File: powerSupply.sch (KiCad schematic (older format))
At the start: 40 parts, among them U10 TPS7A4901, U11 LM3880, U12 TPS7A3001, U13 TPS7A3001, U8 TPS7A4901, U9 TPS7A4901

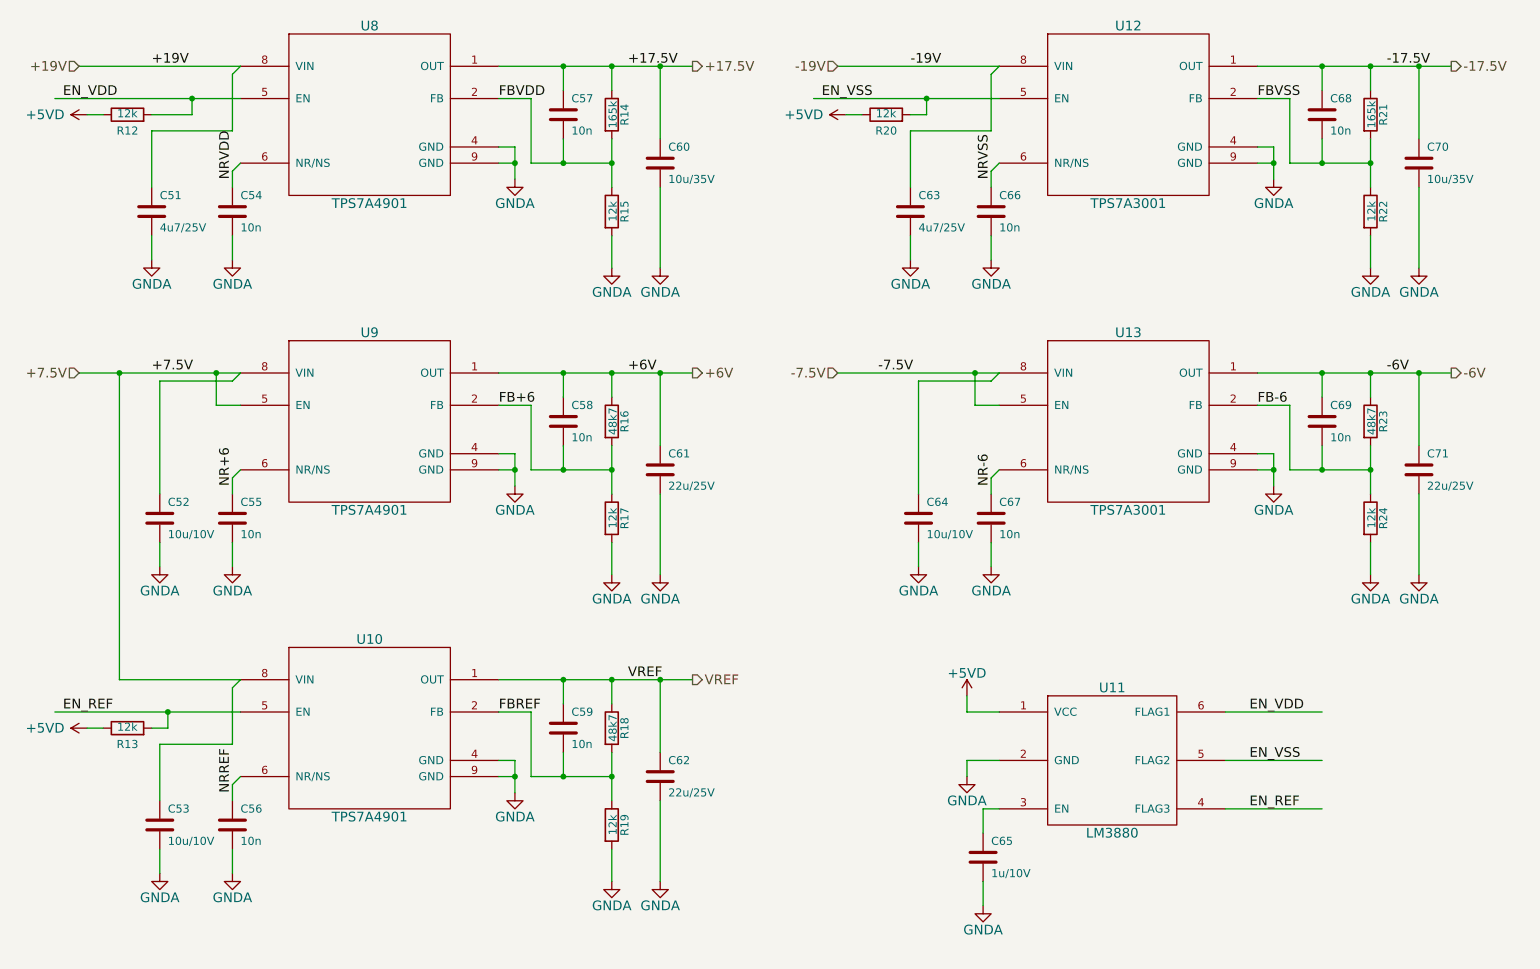
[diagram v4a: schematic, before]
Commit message: Expanded the board for better grounding. OP-AMPs close to connectors
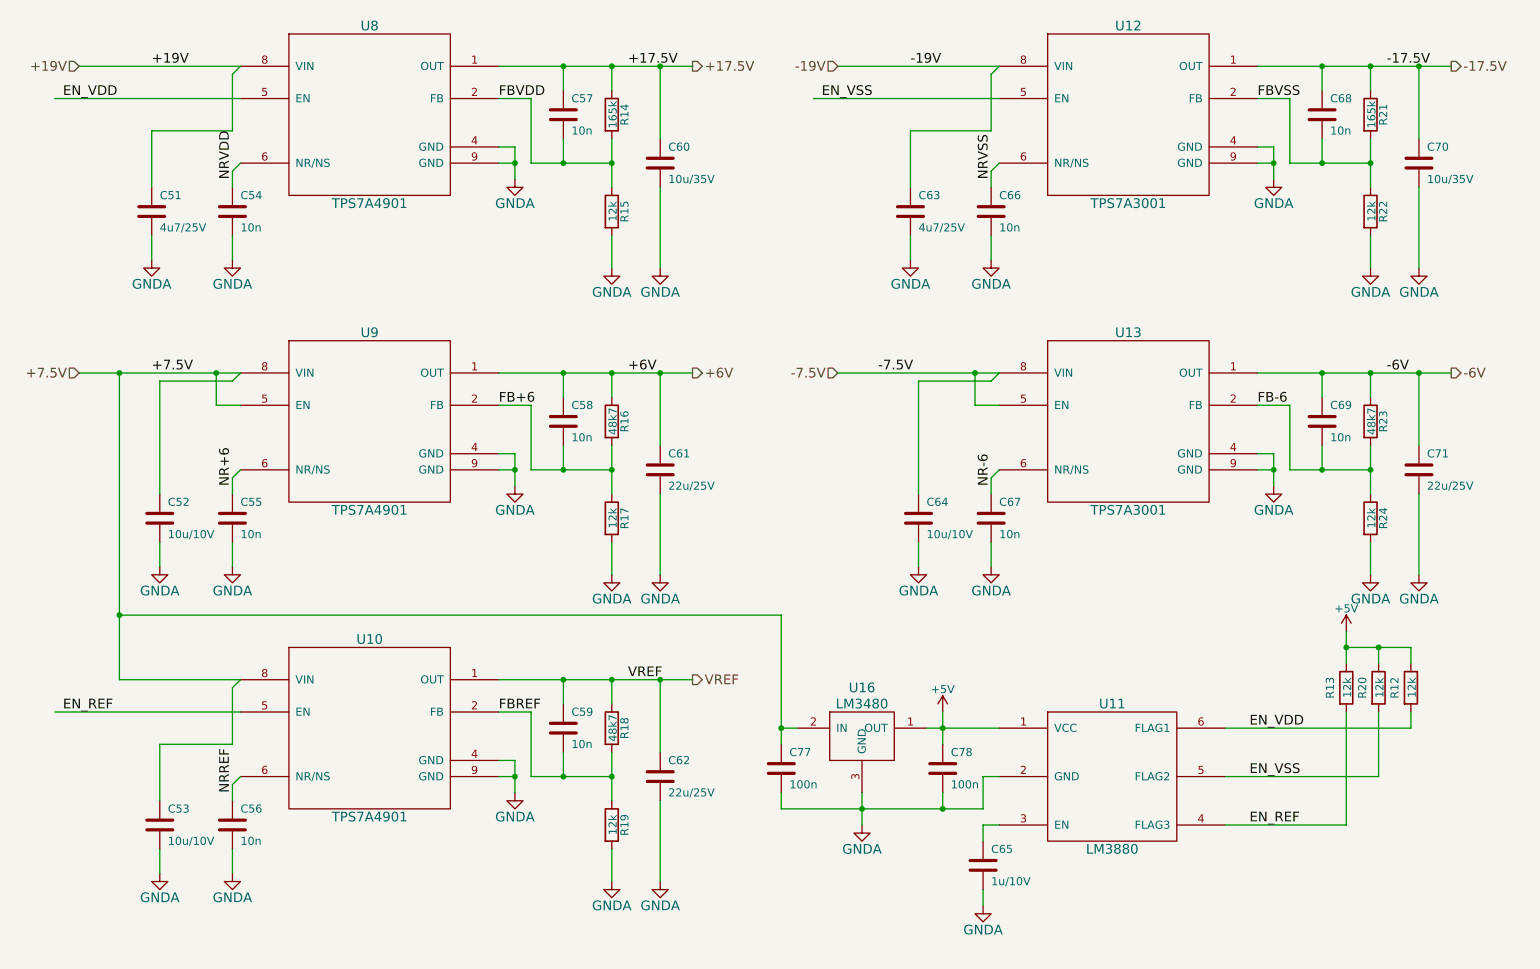
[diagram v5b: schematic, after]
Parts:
- added C77, C78: 100n, Capacitors_SMD:C_0603, symbol C
- added U16: LM3480, TO_SOT_Packages_SMD:SOT-23, symbol LM3480
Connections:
- net labels added: +5V
- net labels removed: +5VD
- wire segments 140 -> 145
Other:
- moved on the sheet: C65, R12, R13, R20, U11

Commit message: Fixed can, 1Ohm resistor descriptions
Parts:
- U16: Alt. Order Code (none) -> 926-LM3480IM3-50; Alt. Supplier (none) -> Mouser; Manufacturer (none) -> Texas Instruments; Note (none) -> 100-mA SOT-23 quasi low-dropout linear voltage regulator; Order Code (none) -> 3160634; Package (none) -> SOT-23; Part Number (none) -> LM3480IM3-5.0; Supplier (none) -> Farnell
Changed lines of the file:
@@
 $EndComp
 $Comp
-L GNDA #PWR053
+L GNDA #PWR056
 U 1 1 5573DDEC
 P 2400 2200
-F 0 "#PWR053" H 2400 1950 60  0001 C CNN
+F 0 "#PWR056" H 2400 1950 60  0001 C CNN
 F 1 "GNDA" H 2400 2050 60  0000 C CNN
 F 2 "" H 2400 2200 60  0000 C CNN
@@
 $EndComp
 $Comp
-L GNDA #PWR054
+L GNDA #PWR057
 U 1 1 5573DE14
 P 2900 2200
-F 0 "#PWR054" H 2900 1950 60  0001 C CNN
+F 0 "#PWR057" H 2900 1950 60  0001 C CNN
 F 1 "GNDA" H 2900 2050 60  0000 C CNN
 F 2 "" H 2900 2200 60  0000 C CNN
@@
 $EndComp
 $Comp
-L GNDA #PWR055
+L GNDA #PWR058
 U 1 1 5573E072
 P 5250 2250
-F 0 "#PWR055" H 5250 2000 60  0001 C CNN
+F 0 "#PWR058" H 5250 2000 60  0001 C CNN
 F 1 "GNDA" H 5250 2100 60  0000 C CNN
 F 2 "" H 5250 2250 60  0000 C CNN
@@
 +17.5V
 $Comp
-L GNDA #PWR056
+L GNDA #PWR059
 U 1 1 5573E1E3
 P 4650 1700
-F 0 "#PWR056" H 4650 1450 60  0001 C CNN
+F 0 "#PWR059" H 4650 1450 60  0001 C CNN
 F 1 "GNDA" H 4650 1550 60  0000 C CNN
 F 2 "" H 4650 1700 60  0000 C CNN
@@
 $EndComp
 $Comp
-L GNDA #PWR057
+L GNDA #PWR060
 U 1 1 5573EA7F
 P 2450 4100
-F 0 "#PWR057" H 2450 3850 60  0001 C CNN
+F 0 "#PWR060" H 2450 3850 60  0001 C CNN
 F 1 "GNDA" H 2450 3950 60  0000 C CNN
 F 2 "" H 2450 4100 60  0000 C CNN
@@
 $EndComp
 $Comp
-L GNDA #PWR058
+L GNDA #PWR061
 U 1 1 5573EA85
 P 2900 4100
-F 0 "#PWR058" H 2900 3850 60  0001 C CNN
+F 0 "#PWR061" H 2900 3850 60  0001 C CNN
 F 1 "GNDA" H 2900 3950 60  0000 C CNN
 F 2 "" H 2900 4100 60  0000 C CNN
@@
 $EndComp
 $Comp
-L GNDA #PWR059
+L GNDA #PWR062
 U 1 1 5573EAA9
 P 5250 4150
-F 0 "#PWR059" H 5250 3900 60  0001 C CNN
+F 0 "#PWR062" H 5250 3900 60  0001 C CNN
 F 1 "GNDA" H 5250 4000 60  0000 C CNN
 F 2 "" H 5250 4150 60  0000 C CNN
@@
 +6V
 $Comp
-L GNDA #PWR060
+L GNDA #PWR063
 U 1 1 5573EAB9
 P 4650 3600
-F 0 "#PWR060" H 4650 3350 60  0001 C CNN
+F 0 "#PWR063" H 4650 3350 60  0001 C CNN
 F 1 "GNDA" H 4650 3450 60  0000 C CNN
 F 2 "" H 4650 3600 60  0000 C CNN
@@
 $EndComp
 $Comp
-L GNDA #PWR061
+L GNDA #PWR064
 U 1 1 5573EE51
 P 2450 6000
-F 0 "#PWR061" H 2450 5750 60  0001 C CNN
+F 0 "#PWR064" H 2450 5750 60  0001 C CNN
 F 1 "GNDA" H 2450 5850 60  0000 C CNN
 F 2 "" H 2450 6000 60  0000 C CNN
@@
 $EndComp
 $Comp
-L GNDA #PWR062
+L GNDA #PWR065
 U 1 1 5573EE57
 P 2900 6000
-F 0 "#PWR062" H 2900 5750 60  0001 C CNN
+F 0 "#PWR065" H 2900 5750 60  0001 C CNN
 F 1 "GNDA" H 2900 5850 60  0000 C CNN
 F 2 "" H 2900 6000 60  0000 C CNN
@@
 $EndComp
 $Comp
-L GNDA #PWR063
+L GNDA #PWR066
 U 1 1 5573EE7B
 P 5250 6050
-F 0 "#PWR063" H 5250 5800 60  0001 C CNN
+F 0 "#PWR066" H 5250 5800 60  0001 C CNN
 F 1 "GNDA" H 5250 5900 60  0000 C CNN
 F 2 "" H 5250 6050 60  0000 C CNN
@@
 VREF
 $Comp
-L GNDA #PWR064
+L GNDA #PWR067
 U 1 1 5573EE8B
 P 4650 5500
-F 0 "#PWR064" H 4650 5250 60  0001 C CNN
+F 0 "#PWR067" H 4650 5250 60  0001 C CNN
 F 1 "GNDA" H 4650 5350 60  0000 C CNN
 F 2 "" H 4650 5500 60  0000 C CNN
@@
 $EndComp
 $Comp
-L GNDA #PWR065
+L GNDA #PWR068
 U 1 1 5573F609
 P 7100 2200
-F 0 "#PWR065" H 7100 1950 60  0001 C CNN
+F 0 "#PWR068" H 7100 1950 60  0001 C CNN
 F 1 "GNDA" H 7100 2050 60  0000 C CNN
 F 2 "" H 7100 2200 60  0000 C CNN
@@
 $EndComp
 $Comp
-L GNDA #PWR066
+L GNDA #PWR069
 U 1 1 5573F60F
 P 7600 2200
-F 0 "#PWR066" H 7600 1950 60  0001 C CNN
+F 0 "#PWR069" H 7600 1950 60  0001 C CNN
 F 1 "GNDA" H 7600 2050 60  0000 C CNN
 F 2 "" H 7600 2200 60  0000 C CNN
@@
 $EndComp
 $Comp
-L GNDA #PWR067
+L GNDA #PWR070
 U 1 1 5573F633
 P 9950 2250
-F 0 "#PWR067" H 9950 2000 60  0001 C CNN
+F 0 "#PWR070" H 9950 2000 60  0001 C CNN
 F 1 "GNDA" H 9950 2100 60  0000 C CNN
 F 2 "" H 9950 2250 60  0000 C CNN
@@
 -17.5V
 $Comp
-L GNDA #PWR068
+L GNDA #PWR071
 U 1 1 5573F643
 P 9350 1700
-F 0 "#PWR068" H 9350 1450 60  0001 C CNN
+F 0 "#PWR071" H 9350 1450 60  0001 C CNN
 F 1 "GNDA" H 9350 1550 60  0000 C CNN
 F 2 "" H 9350 1700 60  0000 C CNN
@@
 $EndComp
 $Comp
-L GNDA #PWR069
+L GNDA #PWR072
 U 1 1 5573F664
 P 7150 4100
-F 0 "#PWR069" H 7150 3850 60  0001 C CNN
+F 0 "#PWR072" H 7150 3850 60  0001 C CNN
 F 1 "GNDA" H 7150 3950 60  0000 C CNN
 F 2 "" H 7150 4100 60  0000 C CNN
@@
 $EndComp
 $Comp
-L GNDA #PWR070
+L GNDA #PWR073
 U 1 1 5573F66A
 P 7600 4100
-F 0 "#PWR070" H 7600 3850 60  0001 C CNN
+F 0 "#PWR073" H 7600 3850 60  0001 C CNN
 F 1 "GNDA" H 7600 3950 60  0000 C CNN
 F 2 "" H 7600 4100 60  0000 C CNN
@@
 $EndComp
 $Comp
-L GNDA #PWR071
+L GNDA #PWR074
 U 1 1 5573F68E
 P 9950 4150
-F 0 "#PWR071" H 9950 3900 60  0001 C CNN
+F 0 "#PWR074" H 9950 3900 60  0001 C CNN
 F 1 "GNDA" H 9950 4000 60  0000 C CNN
 F 2 "" H 9950 4150 60  0000 C CNN
@@
 Text Label 9250 3100 0    60   ~ 0
 FB-6
-Text Label 6900 2900 0    60   ~ 0
+Text Label 7100 2900 0    60   ~ 0
 -7.5V
 Text Label 10050 2900 0    60   ~ 0
 -6V
 $Comp
-L GNDA #PWR072
+L GNDA #PWR075
 U 1 1 5573F69E
 P 9350 3600
-F 0 "#PWR072" H 9350 3350 60  0001 C CNN
+F 0 "#PWR075" H 9350 3350 60  0001 C CNN
 F 1 "GNDA" H 9350 3450 60  0000 C CNN
 F 2 "" H 9350 3600 60  0000 C CNN
@@
 	1800 5000 2950 5000
 Wire Wire Line
-	2200 2900 2200 4800
+	2200 2800 2200 4800
 Wire Wire Line
 	5550 1000 5550 1450
 Connection ~ 5550 1000
 $Comp
-L GNDA #PWR073
+L GNDA #PWR076
 U 1 1 55743F54
 P 5550 2250
-F 0 "#PWR073" H 5550 2000 60  0001 C CNN
+F 0 "#PWR076" H 5550 2000 60  0001 C CNN
 F 1 "GNDA" H 5550 2100 60  0000 C CNN
 F 2 "" H 5550 2250 60  0000 C CNN
@@
 	10250 1000 10250 1450
 $Comp
-L GNDA #PWR074
+L GNDA #PWR077
 U 1 1 557440E7
 P 10250 2250
-F 0 "#PWR074" H 10250 2000 60  0001 C CNN
+F 0 "#PWR077" H 10250 2000 60  0001 C CNN
 F 1 "GNDA" H 10250 2100 60  0000 C CNN
 F 2 "" H 10250 2250 60  0000 C CNN
@@
 	10250 2900 10250 3350
 $Comp
-L GNDA #PWR075
+L GNDA #PWR078
 U 1 1 55744191
 P 10250 4150
-F 0 "#PWR075" H 10250 3900 60  0001 C CNN
+F 0 "#PWR078" H 10250 3900 60  0001 C CNN
 F 1 "GNDA" H 10250 4000 60  0000 C CNN
 F 2 "" H 10250 4150 60  0000 C CNN
@@
 	5550 2900 5550 3350
 $Comp
-L GNDA #PWR076
+L GNDA #PWR079
 U 1 1 5574422F
 P 5550 4150
-F 0 "#PWR076" H 5550 3900 60  0001 C CNN
+F 0 "#PWR079" H 5550 3900 60  0001 C CNN
 F 1 "GNDA" H 5550 4000 60  0000 C CNN
 F 2 "" H 5550 4150 60  0000 C CNN
@@
 	5550 4800 5550 5250
 $Comp
-L GNDA #PWR077
+L GNDA #PWR080
 U 1 1 557442E3
 P 5550 6050
-F 0 "#PWR077" H 5550 5800 60  0001 C CNN
+F 0 "#PWR080" H 5550 5800 60  0001 C CNN
 F 1 "GNDA" H 5550 5900 60  0000 C CNN
 F 2 "" H 5550 6050 60  0000 C CNN
@@
 	2200 4800 2950 4800
 $Comp
-L GNDA #PWR078
+L GNDA #PWR081
 U 1 1 5668CC0B
 P 7550 6200
-F 0 "#PWR078" H 7550 5950 60  0001 C CNN
+F 0 "#PWR081" H 7550 5950 60  0001 C CNN
 F 1 "GNDA" H 7550 6050 60  0000 C CNN
 F 2 "" H 7550 6200 60  0000 C CNN
@@
 $EndComp
 $Comp
-L GNDA #PWR079
+L GNDA #PWR082
 U 1 1 5668CCB6
 P 6800 5700
-F 0 "#PWR079" H 6800 5450 60  0001 C CNN
+F 0 "#PWR082" H 6800 5450 60  0001 C CNN
 F 1 "GNDA" H 6800 5550 60  0000 C CNN
 F 2 "" H 6800 5700 60  0000 C CNN
@@
 F 2 "TO_SOT_Packages_SMD:SOT-23" H 6800 5100 60  0001 C CNN
 F 3 "" H 6800 5100 60  0000 C CNN
+F 4 "LM3480IM3-5.0" H 6800 5100 60  0001 C CNN "Part Number"
+F 5 "Texas Instruments" H 6800 5100 60  0001 C CNN "Manufacturer"
+F 6 "SOT-23" H 6800 5100 60  0001 C CNN "Package"
+F 7 "Farnell" H 6800 5100 60  0001 C CNN "Supplier"
+F 8 "3160634" H 6800 5100 60  0001 C CNN "Order Code"
+F 9 "Mouser" H 6800 5100 60  0001 C CNN "Alt. Supplier"
+F 10 "926-LM3480IM3-50" H 6800 5100 60  0001 C CNN "Alt. Order Code"
+F 11 "100-mA SOT-23 quasi low-dropout linear voltage regulator" H 6800 5100 60  0001 C CNN "Note"
 	1    6800 5100
 	1    0    0    -1
@@
 Connection ~ 7300 5100
 $Comp
-L +5V #PWR080
+L +5V #PWR083
 U 1 1 56E3504C
 P 7300 5000
-F 0 "#PWR080" H 7300 4850 50  0001 C CNN
+F 0 "#PWR083" H 7300 4850 50  0001 C CNN
 F 1 "+5V" H 7300 5140 50  0000 C CNN
 F 2 "" H 7300 5000 50  0000 C CNN
@@
 $EndComp
 $Comp
-L +5V #PWR081
+L +5V #PWR084
 U 1 1 56E350DF
 P 9800 4500
-F 0 "#PWR081" H 9800 4350 50  0001 C CNN
+F 0 "#PWR084" H 9800 4350 50  0001 C CNN
 F 1 "+5V" H 9800 4640 50  0000 C CNN
 F 2 "" H 9800 4500 50  0000 C CNN
@@
 Connection ~ 10000 4600
 Connection ~ 9800 4600
+Wire Wire Line
+	2200 1000 2200 900
+Connection ~ 2200 1000
+$Comp
+L PWR_FLAG #FLG085
+U 1 1 56F228B1
+P 2200 900
+F 0 "#FLG085" H 2200 995 50  0001 C CNN
+F 1 "PWR_FLAG" H 2200 1080 50  0000 C CNN
+F 2 "" H 2200 900 50  0000 C CNN
+F 3 "" H 2200 900 50  0000 C CNN
+	1    2200 900
+	1    0    0    -1
+$EndComp
+$Comp
+L PWR_FLAG #FLG086
+U 1 1 56F22970
+P 2200 2800
+F 0 "#FLG086" H 2200 2895 50  0001 C CNN
+F 1 "PWR_FLAG" H 2200 2980 50  0000 C CNN
+F 2 "" H 2200 2800 50  0000 C CNN
+F 3 "" H 2200 2800 50  0000 C CNN
+	1    2200 2800
+	1    0    0    -1
+$EndComp
+Wire Wire Line
+	6900 1000 6900 900
+$Comp
+L PWR_FLAG #FLG087
+U 1 1 56F22A79
+P 6900 900
+F 0 "#FLG087" H 6900 995 50  0001 C CNN
+F 1 "PWR_FLAG" H 6900 1080 50  0000 C CNN
+F 2 "" H 6900 900 50  0000 C CNN
+F 3 "" H 6900 900 50  0000 C CNN
+	1    6900 900
+	1    0    0    -1
+$EndComp
+Connection ~ 6900 1000
+Wire Wire Line
+	6900 2900 6900 2800
+$Comp
+L PWR_FLAG #FLG088
+U 1 1 56F22C05
+P 6900 2800
+F 0 "#FLG088" H 6900 2895 50  0001 C CNN
+F 1 "PWR_FLAG" H 6900 2980 50  0000 C CNN
+F 2 "" H 6900 2800 50  0000 C CNN
+F 3 "" H 6900 2800 50  0000 C CNN
+	1    6900 2800
+	1    0    0    -1
+$EndComp
+Connection ~ 6900 2900
 $EndSCHEMATC

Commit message: Finalized PCB for production
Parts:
- C51, C63: Alt. Order Code 81-GRM21BR61E475MA2L -> 603-CC805KKX5R8BB475
- C52, C53, C64: Alt. Order Code 81-GRM21BR61A106KE19 -> 603-CC805KKX5R8BB106
- C54, C55, C56, C66, C67: Alt. Order Code 77-VJ0603Y103KXACBC -> 603-CC603KRX7R9BB103; Manufacturer Multicomp -> Yageo; Note 10nF/100V X7R 0603 ceramic capacitor -> 10nF/50V X7R 0603 ceramic capacitor; Order Code 2320786 -> 722236; Part Number MC0603B103K101CT -> CC0603KRX7R9BB103
- C57, C58, C59, C68, C69: Alt. Order Code 77-VJ0603Y103KXACBC -> 603-CC603KRX7R9BB103; Manufacturer Multicomp -> Yageo; Note 10 nF X7R 0603 ceramic capacitor -> 10nF/50V X7R 0603 ceramic capacitor; Order Code 2320786 -> 722236; Part Number MC0603B103K101CT -> CC0603KRX7R9BB103
- C77, C78: Alt. Order Code 710-885012206095 -> 603-CC603KRX7R9BB104; Manufacturer Multicomp -> Yageo; Order Code 1759122 -> 1362556; Part Number MC0603B104K500CT -> CC0603KRX7R9BB104
- R12, R13, R15, R17, R19, R20, R22, R24: footprint Resistors_SMD:R_0805 -> Resistors_SMD:R_0603; Alt. Order Code 667-ERJ-6ENF1202V -> 603-RC0603FR-0712KL; Manufacturer Multicomp -> Yageo; Note 12kΩ/1% 0805 resistor -> 10kΩ/1% 0805 resistor; Order Code 2447563 -> 9238611; Package 0805 -> 0603; Part Number MCWR08X1202FTL -> RC0603FR-0712KL
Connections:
- net +5V: now also R12.2, R13.2, R20.2; no longer R12.1, R13.1, R20.1
- net EN_REF: now also R13.1; no longer R13.2
- net EN_VDD: now also R12.1; no longer R12.2
- net EN_VSS: now also R20.1; no longer R20.2

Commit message: Re-referenced components
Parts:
- removed C63: 4u7/25V, Capacitors_SMD:C_0805, symbol C
- added C65: 10u/25V, Capacitors_SMD:C_0805, symbol C
- C51: value 4u7/25V -> 10u/25V; Alt. Order Code 603-CC805KKX5R8BB475 -> 603-CC805KKX5R8BB106; Note 4.7μF/25V X5R 0805 ceramic capacitor -> 10μF/25V X5R 0805 ceramic capacitor; Order Code 2362111 -> 2426961; Part Number GRM21BR61E475MA12L -> GRM219R61E106KA12D
- C52, C53, C64: value 10u/10V -> 10u/25V; Note 10μF/10V X5R 0805 ceramic capacitor -> 10μF/25V X5R 0805 ceramic capacitor; Order Code 1828805 -> 2426961; Part Number GRM21BR61A106KE19L -> GRM219R61E106KA12D
- C69: renamed from C65; value 1u/10V -> 1u/25V; Alt. Order Code 710-885012106010 -> 603-CC603KRX7R8BB105; Manufacturer Multicomp -> Murata; Note 1μF/10V X5R 0603 ceramic capacitor -> 1μF/25V X7R 0603 ceramic capacitor; Order Code 1759399 -> 2470425; Part Number MC0603X105K100CT -> GCM188R71E105KA64D
- renumbered C77 to C63, C78 to C68, C68 to C70, C69 to C71, C70 to C72, C71 to C73, R14 to R12, R15 to R13, R16 to R14, R17 to R15, R18 to R16, R19 to R17, R21 to R18, R22 to R19, R23 to R20, R24 to R21, R13 to R22, R20 to R23, R12 to R24, U16 to U11, U11 to U14
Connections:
- net -19V: now also C64.1
- net -7.5V: now also C65.1; no longer C64.1
- net GNDA: now also C65.2
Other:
- moved on the sheet: C63, C68, C69, R22, R23, R24, U11, U14
